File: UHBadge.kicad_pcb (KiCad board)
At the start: 2 copper layers, 70 x 117.6 mm, 81 parts, among them J1 Conn_01x03_MountingPin, J2 Conn_01x10_MountingPin, P1 USB_C_Plug_USB2.0, Q1 Si1308EDL, SW1 Boot, SW2 Run, SW3 Up, SW4 Down, SW5 Left, SW6 Right, U1 RP2350A, U2 MCP73871, U3 W25Q128JVS, U4 SRV05-4, U5 Conn, U6 ST25DV64K-JFR6D3, Y1 ABM8-272-T3

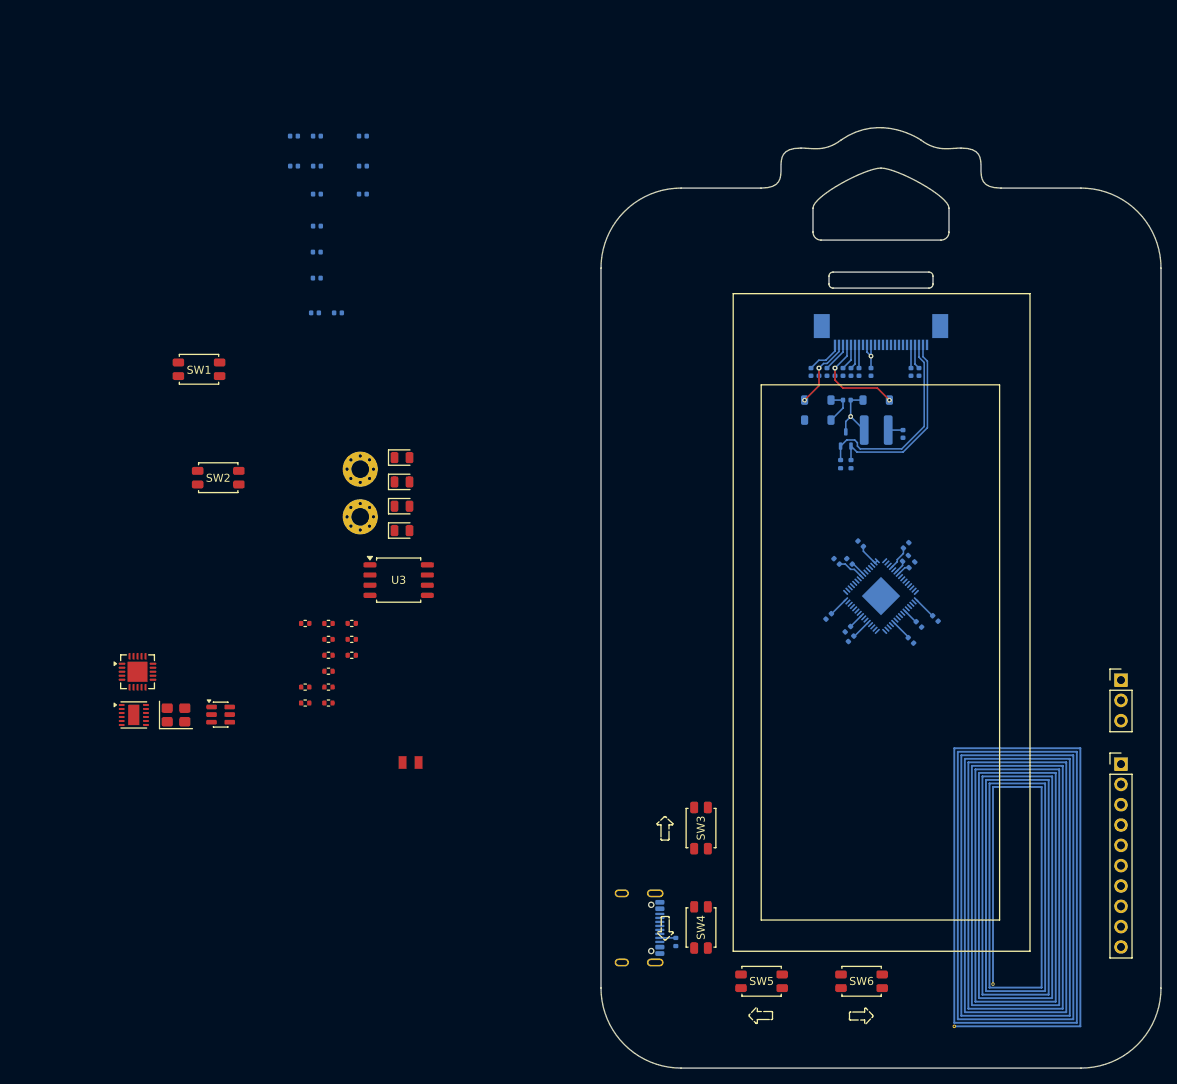
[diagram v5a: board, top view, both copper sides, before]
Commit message: RP2350 Support components placement, USB-C connection and NFC component placement.
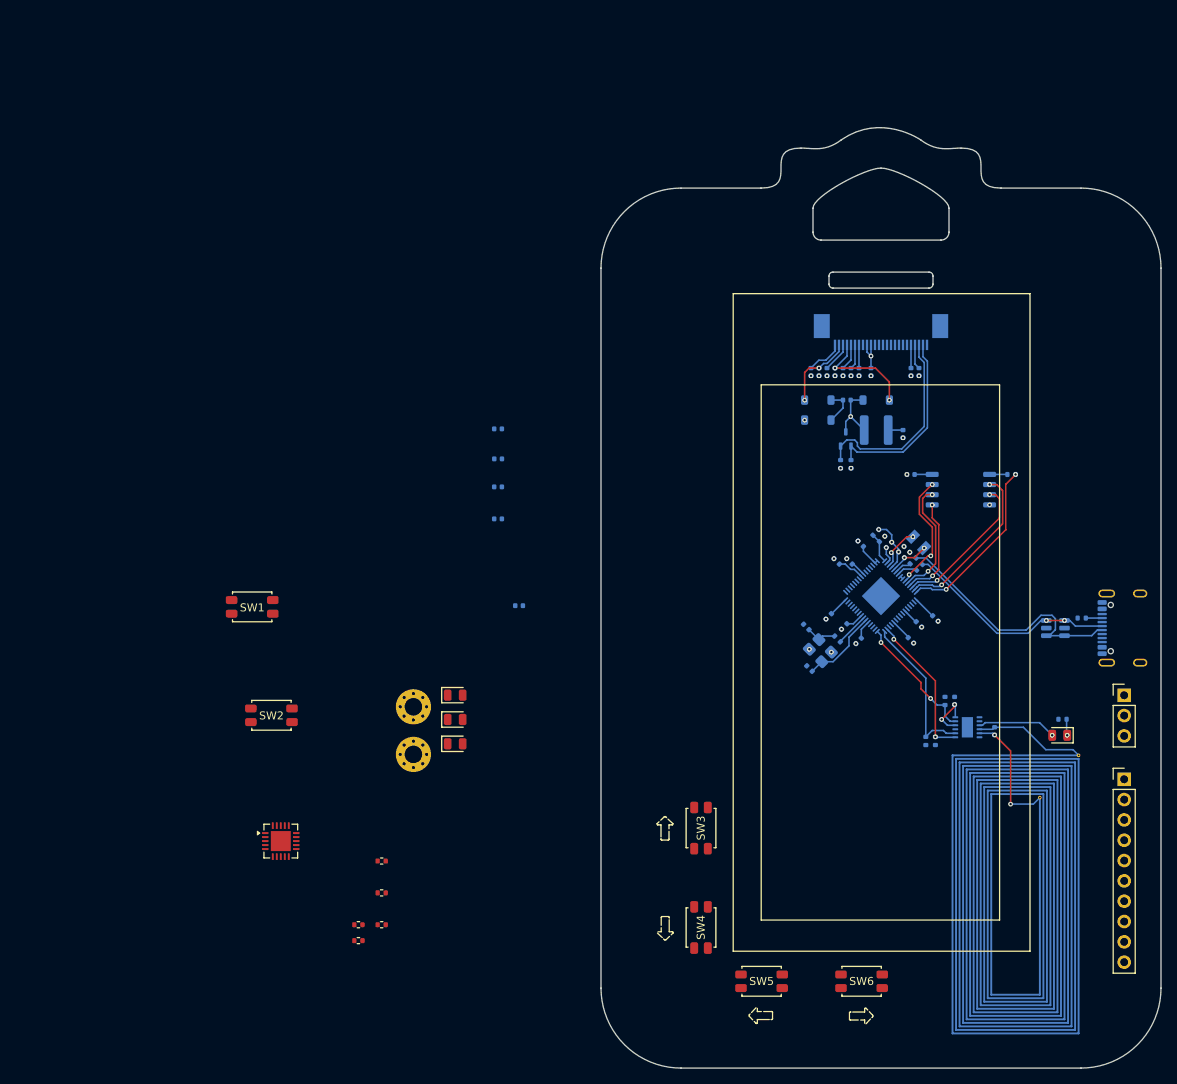
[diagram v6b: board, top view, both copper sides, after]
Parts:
- L1, R1, R10, R12, R13, R14, R15, R8, U3, U4, U6, Y1: moved to B.Cu
- moved C22 114.9 mm to (149.2, 117.9), turned to -90 degrees
- moved C23 106.2 mm to (144.2, 114.1), turned to -90 degrees
- moved U4 104.9 mm to (156.8, 105.0), turned to 180 degrees
- moved U6 104.2 mm to (145.8, 117.4), turned to 180 degrees
- moved R15 89.2 mm to (157.7, 116.4), turned to 180 degrees
- moved R8 87.8 mm to (151.3, 85.8)
- moved D4 86.1 mm to (157.3, 118.4), turned to 180 degrees
- moved C1 82.2 mm to (135.1, 93.9), turned to 45 degrees
- moved C3 81.6 mm to (138.3, 95.9), turned to 45 degrees
- moved C2 81.0 mm to (136.0, 94.6), turned to -135 degrees
- moved Y1 80.9 mm to (127.4, 107.8), turned to 135 degrees
- moved C19 79.3 mm to (138.7, 85.8)
- moved C21 76.1 mm to (126.1, 110.1), turned to -45 degrees
- moved C20 75.1 mm to (125.7, 104.9), turned to 135 degrees
- moved R12 74.8 mm to (140.6, 119.1), turned to 90 degrees
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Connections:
- net RP2350_DECOUPLING_DVDD renamed +1V1
- C1 pad 2: RP2350_VREG_PGND -> -BATT
- C10 pad 1: RP2350_DECOUPLING_IOVDD+ -> +3V3
- C10 pad 2: RP2350_VREG_PGND -> -BATT
- C11 pad 1: RP2350_DECOUPLING_IOVDD+ -> +3V3
- C11 pad 2: RP2350_VREG_PGND -> -BATT
- C12 pad 1: RP2350_DECOUPLING_IOVDD+ -> +3V3
- C12 pad 2: RP2350_VREG_PGND -> -BATT
- C13 pad 1: RP2350_DECOUPLING_IOVDD+ -> +3V3
- C13 pad 2: RP2350_VREG_PGND -> -BATT
- C16 pad 1: RP2350_VREG_PGND -> -BATT
- C16 pad 2: RP2350_DECOUPLING_IOVDD+ -> +3V3
- C17 pad 1: RP2350_VREG_PGND -> -BATT
- C17 pad 2: RP2350_DECOUPLING_IOVDD+ -> +3V3
- C18 pad 2: RP2350_VREG_PGND -> -BATT
- C19 pad 1: RP2350_DECOUPLING_IOVDD+ -> +3V3
- C19 pad 2: RP2350_VREG_PGND -> -BATT
- C2 pad 1: RP2350_DECOUPLING_IOVDD+ -> +3V3
- C2 pad 2: RP2350_VREG_PGND -> -BATT
- C20 pad 2: RP2350_VREG_PGND -> -BATT
- C21 pad 1: RP2350_VREG_PGND -> -BATT
- C23 pad 1: RP2350_VREG_PGND -> -BATT
- C23 pad 2: RP2350_DECOUPLING_IOVDD+ -> +3V3
- C24 pad 1: RP2350_VREG_PGND -> -BATT
- C25 pad 1: RP2350_VREG_PGND -> -BATT
- C26 pad 1: RP2350_VREG_PGND -> -BATT
- C27 pad 1: RP2350_VREG_PGND -> -BATT
- C28 pad 1: RP2350_VREG_PGND -> -BATT
- C29 pad 1: RP2350_VREG_PGND -> -BATT
- C3 pad 2: RP2350_VREG_PGND -> -BATT
- C30 pad 1: RP2350_VREG_PGND -> -BATT
- C31 pad 1: RP2350_VREG_PGND -> -BATT
- C31 pad 2: RP2350_DECOUPLING_IOVDD+ -> +3V3
- C32 pad 1: RP2350_VREG_PGND -> -BATT
- C33 pad 1: RP2350_VREG_PGND -> -BATT
- C34 pad 1: RP2350_DECOUPLING_IOVDD+ -> +3V3
- C34 pad 2: RP2350_VREG_PGND -> -BATT
- C4 pad 2: RP2350_VREG_PGND -> -BATT
- C5 pad 2: RP2350_VREG_PGND -> -BATT
- C6 pad 2: RP2350_VREG_PGND -> -BATT
- C7 pad 1: RP2350_DECOUPLING_IOVDD+ -> +3V3
- C7 pad 2: RP2350_VREG_PGND -> -BATT
- C8 pad 1: RP2350_DECOUPLING_IOVDD+ -> +3V3
- C8 pad 2: RP2350_VREG_PGND -> -BATT
- C9 pad 1: RP2350_DECOUPLING_IOVDD+ -> +3V3
- C9 pad 2: RP2350_VREG_PGND -> -BATT
- D5 pad 1: RP2350_VREG_PGND -> -BATT
- H1 pad 1: RP2350_VREG_PGND -> -BATT
- H2 pad 1: RP2350_VREG_PGND -> -BATT
- J1 pad 2: RP2350_VREG_PGND -> -BATT
- J2 pad 1: RP2350_DECOUPLING_IOVDD+ -> +3V3
- J2 pad 10: RP2350_VREG_PGND -> -BATT
- L3 pad 1: RP2350_DECOUPLING_IOVDD+ -> +3V3
- P1 pad A1: RP2350_VREG_PGND -> -BATT
- P1 pad A12: RP2350_VREG_PGND -> -BATT
- P1 pad B1: RP2350_VREG_PGND -> -BATT
- P1 pad B12: RP2350_VREG_PGND -> -BATT
- P1 pad SH: RP2350_VREG_PGND -> -BATT
- R1 pad 1: RP2350_DECOUPLING_IOVDD+ -> +3V3
- R11 pad 2: RP2350_VREG_PGND -> -BATT
- R12 pad 1: RP2350_DECOUPLING_IOVDD+ -> +3V3
- R13 pad 1: RP2350_DECOUPLING_IOVDD+ -> +3V3
- R14 pad 1: RP2350_DECOUPLING_IOVDD+ -> +3V3
- R15 pad 2: RP2350_VREG_PGND -> -BATT
- R16 pad 1: RP2350_VREG_PGND -> -BATT
- R17 pad 1: RP2350_VREG_PGND -> -BATT
- R4 pad 2: RP2350_VREG_PGND -> -BATT
- SW1 pad 1: RP2350_VREG_PGND -> -BATT
- SW3 pad 2: RP2350_VREG_PGND -> -BATT
- SW4 pad 2: RP2350_VREG_PGND -> -BATT
- SW5 pad 2: RP2350_VREG_PGND -> -BATT
- SW6 pad 2: RP2350_VREG_PGND -> -BATT
- U1 pad 1: RP2350_DECOUPLING_IOVDD+ -> +3V3
- U1 pad 11: RP2350_DECOUPLING_IOVDD+ -> +3V3
- U1 pad 20: RP2350_DECOUPLING_IOVDD+ -> +3V3
- U1 pad 30: RP2350_DECOUPLING_IOVDD+ -> +3V3
- U1 pad 38: RP2350_DECOUPLING_IOVDD+ -> +3V3
- U1 pad 44: RP2350_DECOUPLING_IOVDD+ -> +3V3
- U1 pad 45: RP2350_DECOUPLING_IOVDD+ -> +3V3
- U1 pad 47: RP2350_VREG_PGND -> -BATT
- U1 pad 49: RP2350_DECOUPLING_IOVDD+ -> +3V3
- U1 pad 53: RP2350_DECOUPLING_IOVDD+ -> +3V3
- U1 pad 54: RP2350_DECOUPLING_IOVDD+ -> +3V3
- U1 pad 61: RP2350_VREG_PGND -> -BATT
- U2 pad 1: RP2350_DECOUPLING_IOVDD+ -> +3V3
- U2 pad 10: RP2350_VREG_PGND -> -BATT
- U2 pad 11: RP2350_VREG_PGND -> -BATT
- U2 pad 14: RP2350_DECOUPLING_IOVDD+ -> +3V3
- U2 pad 15: RP2350_DECOUPLING_IOVDD+ -> +3V3
- U2 pad 16: RP2350_DECOUPLING_IOVDD+ -> +3V3
- U2 pad 20: RP2350_DECOUPLING_IOVDD+ -> +3V3
- U2 pad 21: RP2350_VREG_PGND -> -BATT
- U2 pad 3: RP2350_VREG_PGND -> -BATT
- U2 pad 9: RP2350_VREG_PGND -> -BATT
- U3 pad 4: RP2350_VREG_PGND -> -BATT
- U3 pad 8: RP2350_DECOUPLING_IOVDD+ -> +3V3
- U4 pad 2: RP2350_VREG_PGND -> -BATT
- U5 pad 10: RP2350_DECOUPLING_IOVDD+ -> +3V3
- U5 pad 17: RP2350_VREG_PGND -> -BATT
- U5 pad 8: RP2350_VREG_PGND -> -BATT
- U5 pad 9: RP2350_DECOUPLING_IOVDD+ -> +3V3
- U5 pad MP: RP2350_VREG_PGND -> -BATT
- U6 pad 10: RP2350_DECOUPLING_IOVDD+ -> +3V3
- U6 pad 12: RP2350_DECOUPLING_IOVDD+ -> +3V3
- U6 pad 6: RP2350_VREG_PGND -> -BATT
- Y1 pad 2: RP2350_VREG_PGND -> -BATT
- Y1 pad 4: RP2350_VREG_PGND -> -BATT
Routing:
- net +3V3: track 0.00 -> 38.7 mm, vias 0 -> 6
- net USB_C_D-: track 0.00 -> 32.2 mm
- net USB_C_D+: track 0.00 -> 27.0 mm, vias 0 -> 2
- net RP2350_DECOUPLING_IOVDD+: track 26.4 -> 0.00 mm, vias 1 -> 0
- net QSPI_SS: track 0.00 -> 22.0 mm, vias 0 -> 2
- net QSPI_SD1: track 0.00 -> 20.8 mm, vias 0 -> 2
- net NFC_SCL: track 0.00 -> 19.5 mm
- net NFC_SDA: track 0.00 -> 18.5 mm, vias 0 -> 2
- net QSPI_SD2: track 0.00 -> 18.4 mm, vias 0 -> 2
- net NFC_GPO: track 0.00 -> 16.2 mm, vias 0 -> 2
- net Net-(U6-AC1): track 0.00 -> 15.4 mm, vias 0 -> 2
- net QSPI_SD3: track 0.00 -> 15.1 mm, vias 0 -> 3
- net QSPI_SCLK: track 0.00 -> 14.8 mm, vias 0 -> 2
- net Net-(U6-AC0): track 0.00 -> 13.9 mm
- net QSPI_SD0: track 0.00 -> 12.9 mm, vias 0 -> 2
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
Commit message: Battery Port Placement. Finished the recharge system. Placed the mounting holes. Started filling the areas and connecting the components.
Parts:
- removed C14, C15: 100nF, Capacitor_SMD:C_0402_1005Metric
- added J3: LEMO2, Connector_Molex:Molex_CLIK-Mate_502494-0270_1x02-1MP_P2.00mm_Horizontal, B.Cu at (134.9, 144.7)
- D1, D2, D3, R11, R5, R6, R7, R9, SW1, SW2, U2: moved to B.Cu
- moved SW2 106.6 mm to (162.0, 89.0), turned to 180 degrees
- moved SW1 106.0 mm to (162.0, 94.0), turned to 180 degrees
- moved H1 103.5 mm to (162.6, 57.4)
- moved R11 98.9 mm to (156.5, 89.8), turned to 180 degrees
- moved R9 94.4 mm to (156.5, 94.9), turned to 180 degrees
- moved H2 70.5 mm to (107.4, 57.4)
- moved U2 62.0 mm to (121.7, 125.5), turned to 180 degrees
- moved R5 55.1 mm to (123.4, 129.7), turned to -90 degrees
- moved R6 53.3 mm to (121.0, 129.7), turned to -90 degrees
- moved C16 52.3 mm to (124.4, 120.6), turned to -90 degrees
- moved R7 49.8 mm to (122.2, 129.7), turned to -90 degrees
- moved C17 48.3 mm to (117.7, 124.7), turned to 0 degrees
- moved D1 47.2 mm to (124.6, 133.3), turned to -90 degrees
- moved C18 46.4 mm to (123.2, 120.6), turned to 90 degrees
- moved D3 42.7 mm to (122.2, 133.3), turned to -90 degrees
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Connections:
- R9 pad 2: QSPI_SS -> -BATT
- SW1 pad 1: -BATT -> QSPI_SS
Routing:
- net USB_C_VBUS: track 0.00 -> 149.8 mm, vias 0 -> 5
- net -BATT: track 2.25 -> 86.2 mm, vias 31 -> 54
- net +3V3: track 38.7 -> 69.3 mm, vias 6 -> 9
- net Net-(R9-Pad1): track 0.00 -> 7.55 mm
- net Net-(R11-Pad1): track 0.00 -> 7.52 mm
- net RIGHT: track 0.00 -> 5.15 mm
- net QSPI_SS: track 22.0 -> 27.1 mm
- net LEFT: track 0.00 -> 5.15 mm
- net DOWN: track 0.00 -> 5.15 mm
- net UP: track 0.00 -> 5.15 mm
- net RUN: track 0.00 -> 5.15 mm
- net Net-(D4-A): track 9.88 -> 7.14 mm
- net Net-(D2-K): track 0.00 -> 2.68 mm
- net Net-(D1-K): track 0.00 -> 2.68 mm
- net NFC_SCL: track 19.5 -> 16.9 mm
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- added copper zone on B.Cu, net -BATT
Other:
- board text added: "3v3"
- board text added: "ADC0"
- board text added: "ADC1"
- board text added: "BOOT"
- board text added: "Battery"
- board text added: "FLASH"
- board text added: "GND"
- board text added: "GPIO0"
- board text added: "GPIO1"
- board text added: "GPIO2"
- board text added: "GPIO3"
- board text added: "GPIO4"
- board text added: "GPIO5"
- board text added: "NFC"
- board text added: "RUN"
- board text added: "SWCLK"
- board text added: "SWDIO"

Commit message: Connected the components together.
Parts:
- moved C34 0.96 mm to (137.8, 79.8), turned to 90 degrees
- moved C12 0.28 mm to (132.0, 106.4)
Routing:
- net -BATT: track 86.2 -> 291.4 mm, vias 54 -> 77
- net +3V3: track 69.3 -> 213.2 mm, vias 9 -> 23
- net RIGHT: track 5.15 -> 79.1 mm, vias 0 -> 2
- net E-INK_BUSY: track 0.00 -> 69.0 mm, vias 0 -> 2
- net E-INK_RST: track 0.00 -> 66.4 mm, vias 0 -> 2
- net E-INK_D/C: track 0.00 -> 65.2 mm, vias 0 -> 2
- net LEFT: track 5.15 -> 62.8 mm, vias 0 -> 2
- net E-INK_CS: track 0.00 -> 54.2 mm, vias 0 -> 2
- net RUN: track 5.15 -> 59.0 mm, vias 0 -> 6
- net E-INK_SCL: track 0.00 -> 52.8 mm, vias 0 -> 2
- net E-INK_SDA: track 0.00 -> 51.3 mm, vias 0 -> 2
- net DOWN: track 5.15 -> 51.8 mm, vias 0 -> 2
- net UP: track 5.15 -> 39.1 mm, vias 0 -> 2
- net +1V1: track 11.2 -> 32.8 mm, vias 2 -> 6
- net QSPI_SS: track 27.1 -> 48.0 mm
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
